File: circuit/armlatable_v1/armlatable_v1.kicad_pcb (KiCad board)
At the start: 2 copper layers, 47 x 36 mm, 24 parts, among them J1 Conn_01x02_Pin, J2 Xiao ESP32S3, J3 Conn_01x04_Socket, J4 Conn_01x04_Socket, J6 Conn_01x02_Socket, J7 Conn_01x02_Socket, Q1 Q_Dual_PMOS_S1G1S2G2D2D2D1D1, SW1 SW_SPDT, U1 TSR0.5-2450, U2 MAX485E

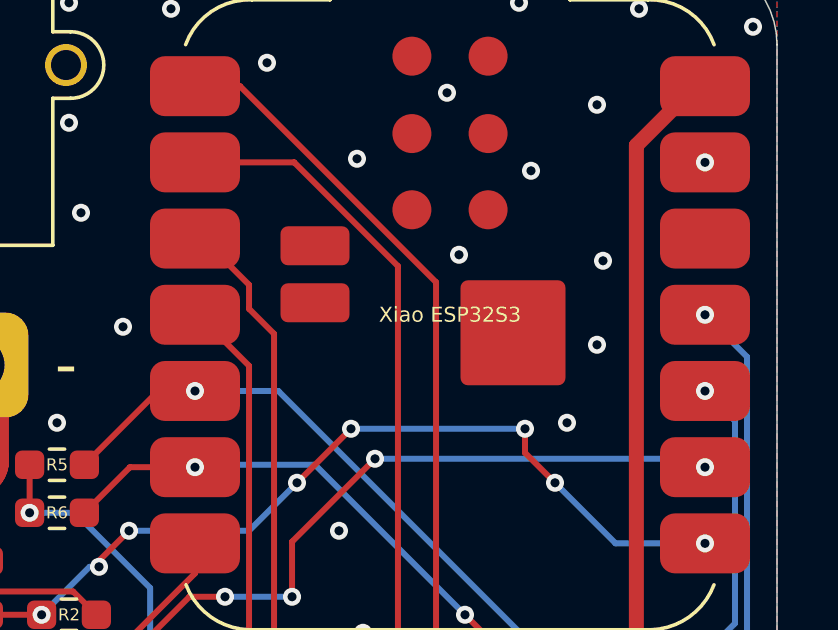
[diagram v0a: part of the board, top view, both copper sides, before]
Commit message: Modify silks
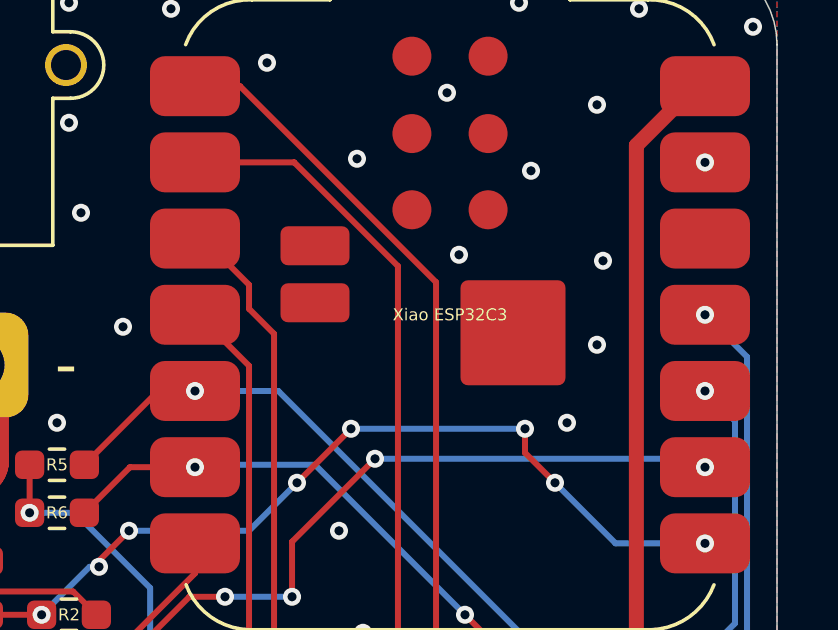
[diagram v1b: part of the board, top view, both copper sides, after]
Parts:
- J2: value Xiao ESP32S3 -> Xiao ESP32C3
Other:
- board text added: "2026/02/01"
- board text added: "Armlatable Main Board V1"
- board text added: "Ueda Toshiaki"
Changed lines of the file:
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@@
 		(allow_soldermask_bridges_in_footprints no)
 		(tenting front back)
+		(aux_axis_origin 100 136)
 		(pcbplotparams
 			(layerselection 0x00000000_00000000_55555555_5755f5ff)
@@
 			)
 		)
-		(property "Value" "Xiao ESP32S3"
+		(property "Value" "Xiao ESP32C3"
 			(at 0 0 0)
 			(unlocked yes)
@@
 			(effects
 				(font
-					(size 0.5 0.5)
-					(thickness 0.08)
+					(size 0.4 0.4)
+					(thickness 0.06)
 				)
 			)
@@
 		(layer "Edge.Cuts")
 	)
+	(gr_text "2026/02/01"
+		(at 145 103 0)
+		(layer "B.SilkS")
+		(effects
+			(font
+				(size 1 1)
+				(thickness 0.1)
+			)
+			(justify left bottom mirror)
+		)
+	)
+	(gr_text "Ueda Toshiaki"
+		(at 145 105 0)
+		(layer "B.SilkS")
+		(effects
+			(font
+				(size 1 1)
+				(thickness 0.1)
+			)
+			(justify left bottom mirror)
+		)
+	)
+	(gr_text "Armlatable Main Board V1"
+		(at 145 107 0)
+		(layer "B.SilkS")
+		(effects
+			(font
+				(size 1 1)
+				(thickness 0.1)
+			)
+			(justify left bottom mirror)
+		)
+	)
 	(segment

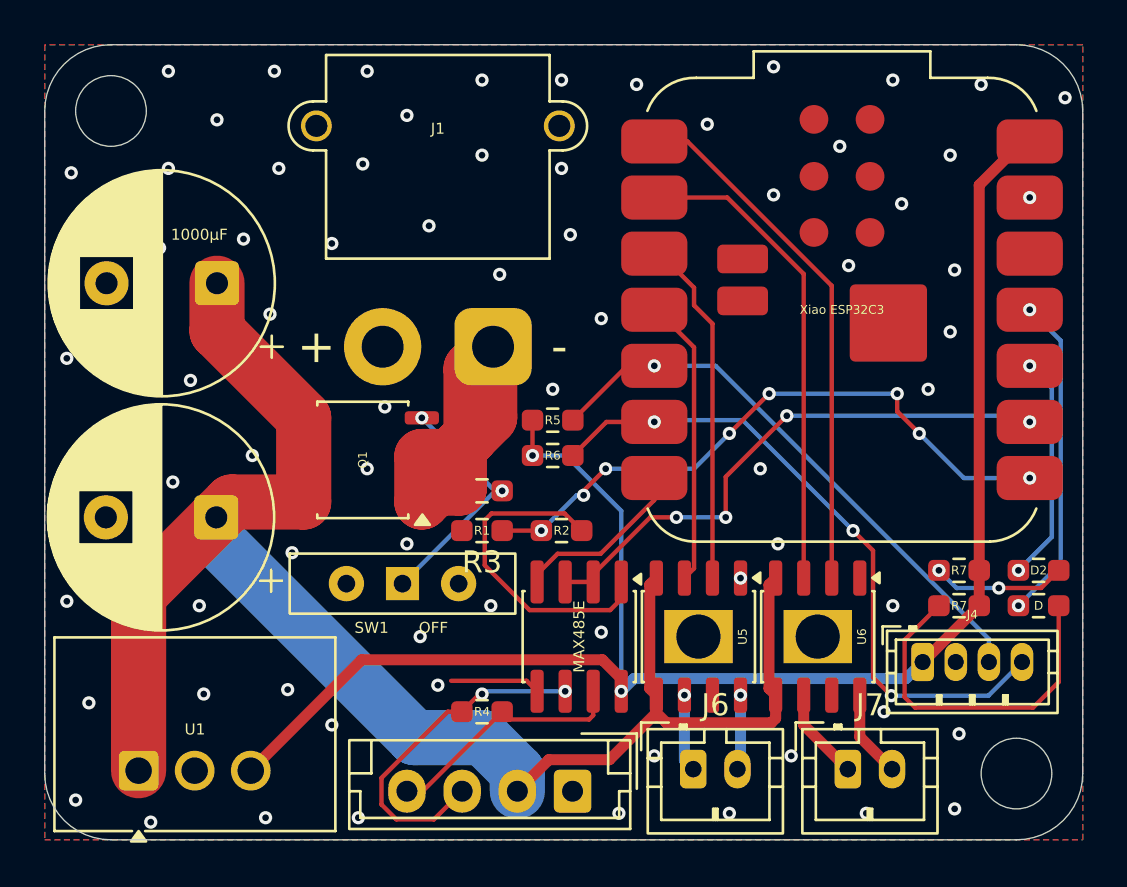
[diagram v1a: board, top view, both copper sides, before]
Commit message: Modify silks
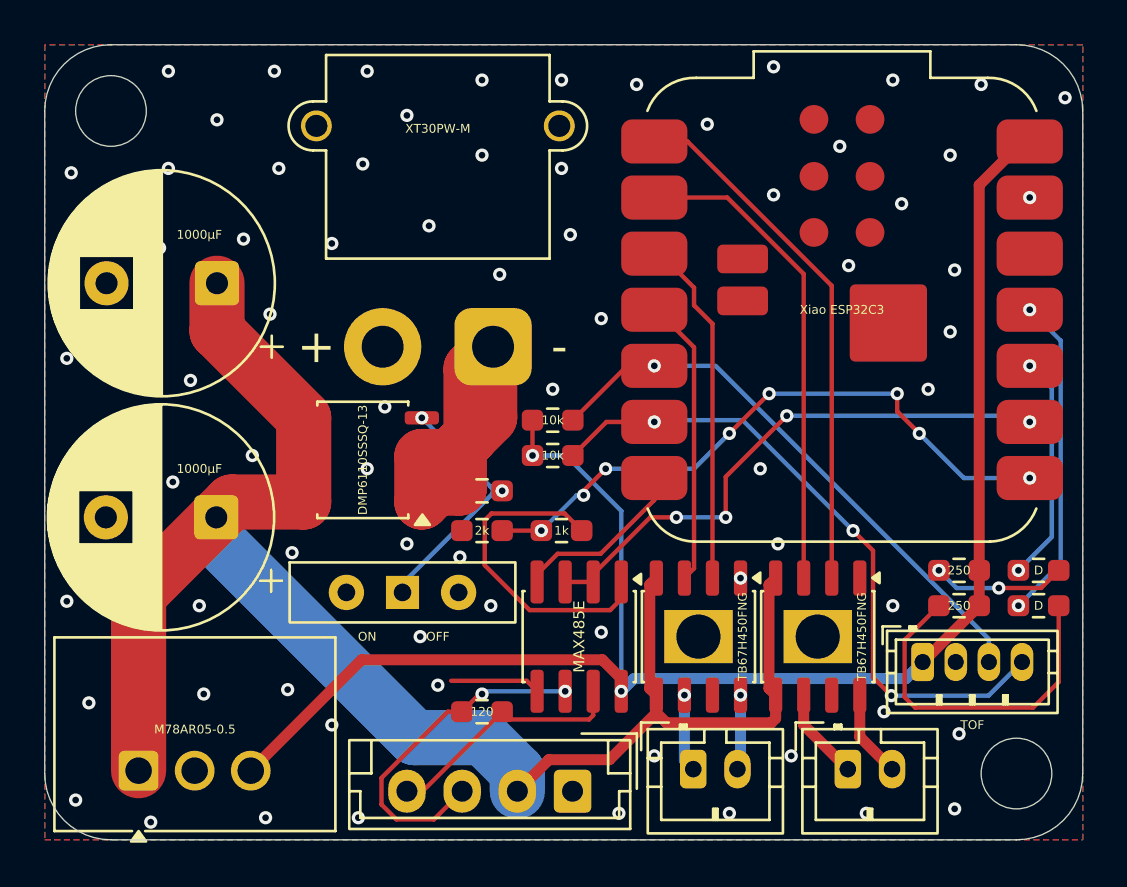
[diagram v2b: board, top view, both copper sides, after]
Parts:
- moved ON 0.40 mm to (116.2, 124.8)
- renumbered R5 to 10k, R6 to 10k, R4 to 120, R2 to 1k, Q1 to DMP6110SSSQ-13, U1 to M78AR05-0.5, SW1 to ON, U6 to TB67H450FNG, U5 to TB67H450FNG, J1 to XT30PW-M
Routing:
- net Net-(Q1A-G): track 11.3 -> 12.0 mm
- net GND: vias 72 -> 73
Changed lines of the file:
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@@
 			(plotframeref no)
 			(mode 1)
-			(useauxorigin no)
+			(useauxorigin yes)
 			(hpglpennumber 1)
 			(hpglpenspeed 20)
@@
 			(outputformat 1)
 			(mirror no)
-			(drillshape 1)
+			(drillshape 0)
 			(scaleselection 1)
-			(outputdirectory "")
+			(outputdirectory "garbar/")
 		)
 	)
@@
 			(at 2.25 -2.15 0)
 			(layer "F.SilkS")
+			(hide yes)
 			(effects
 				(font
@@
 			(layer "F.Fab")
 		)
-		(fp_text user "${REFERENCE}"
-			(at 2.25 1.5 0)
-			(layer "F.Fab")
+		(fp_text user "TOF"
+			(at 2.25 2.85 0)
+			(layer "F.SilkS")
 			(effects
 				(font
-					(size 1 1)
-					(thickness 0.15)
+					(size 0.4 0.4)
+					(thickness 0.06)
 				)
 			)
@@
 			(at 1 -2.9 0)
 			(layer "F.SilkS")
+			(hide yes)
 			(effects
 				(font
@@
 			(at 0 -1.8 0)
 			(layer "F.SilkS")
+			(hide yes)
 			(effects
 				(font
@@
 			(layer "F.Fab")
 		)
-		(fp_text user "${REFERENCE}"
+		(fp_text user "250"
 			(at 0 0 0)
-			(layer "F.Fab")
+			(layer "F.SilkS")
 			(effects
 				(font
@@
 		(descr "SSOP, 8 Pin (https://www.fujitsu.com/uk/Images/MB85RS16.pdf), generated with kicad-footprint-generator ipc_gullwing_generator.py")
 		(tags "SSOP SO")
-		(property "Reference" "Q1"
+		(property "Reference" "DMP6110SSSQ-13"
 			(at 0 0 90)
 			(layer "F.SilkS")
@@
 		(property "Value" "1000μF"
 			(at 0.767677 2.2 0)
-			(layer "F.Fab")
+			(layer "F.SilkS")
 			(effects
 				(font
-					(size 0.5 0.5)
-					(thickness 0.08)
+					(size 0.4 0.4)
+					(thickness 0.06)
 				)
 			)
@@
 			(layer "F.Fab")
 		)
-		(fp_text user "${REFERENCE}"
-			(at 2.5 0 0)
-			(layer "F.Fab")
-			(effects
-				(font
-					(size 1 1)
-					(thickness 0.15)
-				)
-			)
-		)
 		(pad "1" thru_hole roundrect
 			(at 0 0 180)
@@
 			(at 0 -1.43 0)
 			(layer "F.SilkS")
+			(hide yes)
 			(effects
 				(font
@@
 			(layer "F.Fab")
 		)
-		(fp_text user "${REFERENCE}"
+		(fp_text user "2k"
 			(at 0 0 0)
-			(layer "F.Fab")
+			(layer "F.SilkS")
 			(effects
 				(font
@@
 		(descr "Resistor SMD 0603 (1608 Metric), square (rectangular) end terminal, IPC-7351 nominal with elongated pad for handsoldering. (Body size source: IPC-SM-782 page 72, https://www.pcb-3d.com/wordpress/wp-content/uploads/ipc-sm-782a_amendment_1_and_2.pdf), generated with kicad-footprint-generator")
 		(tags "resistor handsolder")
-		(property "Reference" "R5"
+		(property "Reference" "10k"
 			(at 0 0 0)
 			(layer "F.SilkS")
@@
 			(effects
 				(font
-					(size 0.5 0.5)
-					(thickness 0.08)
+					(size 0.4 0.4)
+					(thickness 0.06)
 				)
 			)
@@
 			(layer "F.Fab")
 		)
-		(fp_text user "${REFERENCE}"
-			(at 2.5 0 0)
-			(layer "F.Fab")
-			(effects
-				(font
-					(size 1 1)
-					(thickness 0.15)
-				)
-			)
-		)
 		(pad "1" thru_hole roundrect
 			(at 0 0 180)
@@
 			(layer "F.Fab")
 		)
-		(fp_text user "${REFERENCE}"
-			(at 3.75 1.5 0)
-			(layer "F.Fab")
-			(effects
-				(font
-					(size 1 1)
-					(thickness 0.15)
-				)
-			)
-		)
 		(pad "1" thru_hole roundrect
 			(at 0 0 180)
@@
 		(descr "Resistor SMD 0603 (1608 Metric), square (rectangular) end terminal, IPC-7351 nominal with elongated pad for handsoldering. (Body size source: IPC-SM-782 page 72, https://www.pcb-3d.com/wordpress/wp-content/uploads/ipc-sm-782a_amendment_1_and_2.pdf), generated with kicad-footprint-generator")
 		(tags "resistor handsolder")
-		(property "Reference" "R6"
+		(property "Reference" "10k"
 			(at 0 0 0)
 			(layer "F.SilkS")
@@
 			(at 0 0 0)
 			(layer "F.SilkS")
+			(hide yes)
 			(effects
 				(font
@@
 			(layer "F.Fab")
 		)
-		(fp_text user "${REFERENCE}"
+		(fp_text user "D"
 			(at 0 0 0)
-			(layer "F.Fab")
+			(layer "F.SilkS")
 			(effects
 				(font
@@
 		(descr "HSOP, 8 Pin (https://www.st.com/resource/en/datasheet/l5973d.pdf), generated with kicad-footprint-generator ipc_gullwing_generator.py")
 		(tags "HSOP SO")
-		(property "Reference" "U6"
+		(property "Reference" "TB67H450FNG"
 			(at 0 -2 90)
 			(layer "F.SilkS")
@@
 			(at 1 -2.9 0)
 			(layer "F.SilkS")
+			(hide yes)
 			(effects
 				(font
@@
 			(at 0 -1.6 0)
 			(layer "F.SilkS")
+			(hide yes)
 			(effects
 				(font
@@
 			(layer "F.Fab")
 		)
-		(fp_text user "${REFERENCE}"
+		(fp_text user "250"
 			(at 0 0 0)
 			(layer "F.SilkS")
@@
 		(descr "HSOP, 8 Pin (https://www.st.com/resource/en/datasheet/l5973d.pdf), generated with kicad-footprint-generator ipc_gullwing_generator.py")
 		(tags "HSOP SO")
-		(property "Reference" "U5"
+		(property "Reference" "TB67H450FNG"
 			(at 0 -2 90)
 			(layer "F.SilkS")
@@
 		(descr "Connector XT30 Horizontal PCB Male, https://www.tme.eu/Document/6eb2005a51a52592b3f19e8a450c54c8/XT30PW-M.pdf")
 		(tags "RC Connector XT30")
-		(property "Reference" "J1"
+		(property "Reference" "XT30PW-M"
 			(at -2.5 -9.875 0)
 			(layer "F.SilkS")
 			(effects
 				(font
-					(size 0.5 0.5)
-					(thickness 0.08)
+					(size 0.4 0.4)
+					(thickness 0.06)
 				)
 			)
@@
 		(descr "Resistor SMD 0603 (1608 Metric), square (rectangular) end terminal, IPC-7351 nominal with elongated pad for handsoldering. (Body size source: IPC-SM-782 page 72, https://www.pcb-3d.com/wordpress/wp-content/uploads/ipc-sm-782a_amendment_1_and_2.pdf), generated with kicad-footprint-generator")
 		(tags "resistor handsolder")
-		(property "Reference" "R2"
+		(property "Reference" "1k"
 			(at 0 0 0)
 			(layer "F.SilkS")
@@
 		(descr "Resistor SMD 0603 (1608 Metric), square (rectangular) end terminal, IPC-7351 nominal with elongated pad for handsoldering. (Body size source: IPC-SM-782 page 72, https://www.pcb-3d.com/wordpress/wp-content/uploads/ipc-sm-782a_amendment_1_and_2.pdf), generated with kicad-footprint-generator")
 		(tags "resistor handsolder")
-		(property "Reference" "R4"
+		(property "Reference" "120"
 			(at 0 0 0)
 			(layer "F.SilkS")
@@
 			(layer "F.Fab")
 		)
-		(fp_text user "${REFERENCE}"
-			(at 0 0 0)
-			(layer "F.Fab")
-			(effects
-				(font
-					(size 1 1)
-					(thickness 0.15)
-				)
-			)
-		)
 		(pad "1" smd roundrect
 			(at -2.475 -1.905 270)
@@
 	(footprint "Button_Switch_THT:SW_Slide-03_Wuerth-WS-SLTV_10x2.5x6.4_P2.54mm"
 		(layer "F.Cu")
-		(at 116.2 124.4)
+		(at 116.2 124.8)
 		(descr "Wuerth, WS-SLTV, 450301014042, https://www.we-online.com/components/products/datasheet/450301014042.pdf")
 		(tags "switch single-pole opposite-side-connection double-throw SPDT würth wurth")
-		(property "Reference" "SW1"
-			(at -1.4 2 0)
+		(property "Reference" "ON"
+			(at -1.6 2 0)
 			(layer "F.SilkS")
 			(effects
 				(font
-					(size 0.5 0.5)
-					(thickness 0.08)
+					(size 0.4 0.4)
+					(thickness 0.06)
 				)
 			)
@@
 		)
 		(fp_text user "OFF"
-			(at 1.4 2 0)
+			(at 1.6 2 0)
 			(layer "F.SilkS")
 			(effects
 				(font
-					(size 0.5 0.5)
-					(thickness 0.08)
+					(size 0.4 0.4)
+					(thickness 0.06)
 				)
 			)
@@
 		(descr "DCDC-Converter, TRACO, TSR0.5-24xx, TSR0.5-24xxx, 0.5A, Rev. February 11. 2025, https://www.tracopower.com/products/tsr0.5.pdf, generated with kicad-footprint-generator StandardBox_generator.py")
 		(tags "DCDC-Converter SWITCHING-REGULATOR STEP-DOWN TRACO TSR0.5 2.54MM THT SIP-3 0.5A")
-		(property "Reference" "U1"
+		(property "Reference" "M78AR05-0.5"
 			(at 1.87 2.55 180)
 			(layer "F.SilkS")
 			(effects
 				(font
-					(size 0.5 0.5)
-					(thickness 0.08)
+					(size 0.4 0.4)
+					(thickness 0.06)
 				)
 			)
@@
 	)
 	(via
+		(at 118.8 123.2)
+		(size 0.6)
+		(drill 0.3)
+		(layers "F.Cu" "B.Cu")
+		(free yes)
+		(net 1)
+	)
+	(via
 		(at 110 135)
 		(size 0.6)
@@
 	)
 	(segment
+		(start 120.19 120.01)
+		(end 117.075 116.895)
+		(width 0.2)
+		(layer "B.Cu")
+		(net 8)
+	)
+	(segment
 		(start 116.2 124.4)
-		(end 120.4 120.2)
+		(end 120.29 120.31)
 		(width 0.2)
 		(layer "B.Cu")
@@
 	(segment
 		(start 120.38 120.2)
-		(end 117.075 116.895)
+		(end 120.19 120.01)
+		(width 0.2)
+		(layer "B.Cu")
+		(net 8)
+	)
+	(segment
+		(start 116.2 124.8)
+		(end 116.2 124.4)
+		(width 0.2)
+		(layer "B.Cu")
+		(net 8)
+	)
+	(segment
+		(start 120.29 120.11)
+		(end 120.29 120.31)
+		(width 0.2)
+		(layer "B.Cu")
+		(net 8)
+	)
+	(segment
+		(start 120.29 120.31)
+		(end 120.4 120.2)
 		(width 0.2)
 		(layer "B.Cu")
@@
 		(width 0.2)
 		(layer "B.Cu")
+		(net 8)
+	)
+	(segment
+		(start 120.19 120.01)
+		(end 120.29 120.11)
+		(width 0.2)
+		(layer "B.Cu")

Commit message: fix: Modify circuit
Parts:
- AM2837, U6: renamed from TB67H450FNG; footprint Package_SO:HSOP-8-1EP_3.9x4.9mm_P1.27mm_EP2.41x3.1mm -> Package_SO:SO-8_3.9x4.9mm_P1.27mm
- J2: value Xiao ESP32C3 -> Xiao ESP32S3
- J3: value Conn_01x04_Socket -> DXL
- R1: value 10kΩ -> 103
- R3: value 2kΩ -> 2.2kΩ
- R7, R8: value 250Ω -> 430Ω
- moved DMP6110 0.80 mm to (114.4, 119.6)
- moved J6 0.25 mm to (129.4, 133.1)
- moved J7 0.20 mm to (136.4, 133.0)
- renumbered 1k to 102, 10k to 103, 120 to 121, DMP6110SSSQ-13 to DMP6110, XT30PW-M to XT30
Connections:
- AM2837 pad 1: GND -> MD1INA
- AM2837 pad 2: MD1INA -> MD1INB
- AM2837 pad 3: MD1INB -> GND
- AM2837 pad 5: +12V -> Net-(J6-Pin_2)
- AM2837 pad 7: unconnected-(U5-RS-Pad7) -> Net-(J6-Pin_1)
- U6 pad 1: GND -> MD2INA
- U6 pad 2: MD2INA -> MD2INB
- U6 pad 3: MD2INB -> GND
- U6 pad 5: +12V -> Net-(J7-Pin_2)
- U6 pad 7: unconnected-(U6-RS-Pad7) -> Net-(J7-Pin_1)
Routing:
- net GND: track 4.09 -> 13.9 mm, vias 73 -> 68
- net Net-(J1-Pin_1): track 18.1 -> 9.95 mm
- net Net-(J6-Pin_1): track 3.41 -> 5.54 mm
- net Net-(J6-Pin_2): track 3.52 -> 5.60 mm
- net Net-(J7-Pin_1): track 3.95 -> 6.03 mm
- net +12V: track 75.0 -> 73.0 mm
- net Net-(J7-Pin_2): track 4.18 -> 5.65 mm
- net RDE: track 25.5 -> 24.5 mm
- net MD1INA: track 15.9 -> 16.9 mm
- net MD1INB: track 13.1 -> 14.1 mm
- net RX: track 28.7 -> 28.1 mm
- net Net-(J3-Pin_3): track 15.6 -> 16.2 mm
- net MD2INA: track 24.0 -> 24.5 mm
- net MD2INB: track 22.0 -> 22.5 mm
- net Net-(Q1A-G): track 12.0 -> 11.5 mm, vias 2 -> 1
